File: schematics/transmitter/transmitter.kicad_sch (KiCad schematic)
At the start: 24 parts, among them Q1 2N7000, SW1 SW_Nidec_CAS-120A1, U1 PIC16F18324-xSL, U2 NRF24L01_Breakout, U3 LM2937xT

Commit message: Create gerber files and order
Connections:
- net GND: no longer RV3.S1, RV3.S2
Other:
- moved on the sheet: D1, Q1, R1, RV3

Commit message: Update
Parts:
- U3: Mfn (none) -> Texas Instruments; Mfn PN (none) -> LM2937ET-3.3/NOPB; Supplier (none) -> DigiKey; Supplier PN (none) -> LM2937ET-3.3/NOPB-ND
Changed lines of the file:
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@@
 			)
 		)
-		(property "Datasheet" "http://www.ti.com/lit/ds/symlink/lm2937.pdf"
+		(property "Datasheet" "https://www.ti.com/lit/ds/symlink/lm2937.pdf"
 			(at 133.35 130.81 0)
 			(effects
@@
 			)
 		)
-		(property "Description" "500-mA Low Dropout Regulator, TO-220"
+		(property "Description" "IC REG LINEAR 3.3V 500MA TO220-3"
 			(at 133.35 129.54 0)
 			(effects
@@
 			)
 		)
-		(property "Mfn" ""
+		(property "Mfn" "Texas Instruments"
 			(at 133.35 129.54 0)
 			(effects
@@
 			)
 		)
-		(property "Mfn PN" ""
+		(property "Mfn PN" "LM2937ET-3.3/NOPB"
 			(at 133.35 129.54 0)
 			(effects
@@
 			)
 		)
-		(property "Supplier" ""
+		(property "Supplier" "DigiKey"
 			(at 133.35 129.54 0)
 			(effects
@@
 			)
 		)
-		(property "Supplier PN" ""
+		(property "Supplier PN" "LM2937ET-3.3/NOPB-ND"
 			(at 133.35 129.54 0)
 			(effects

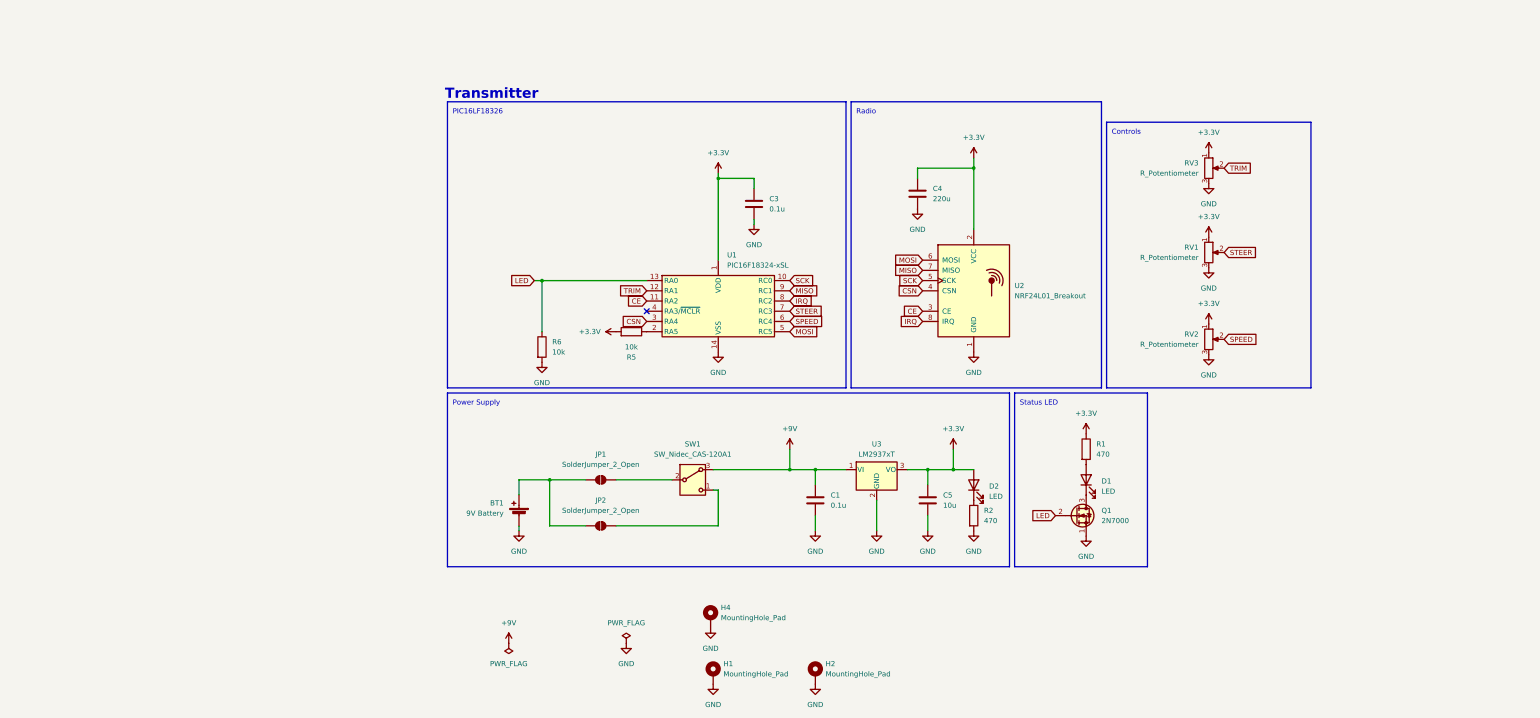
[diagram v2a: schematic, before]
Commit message: Update schematics and their images
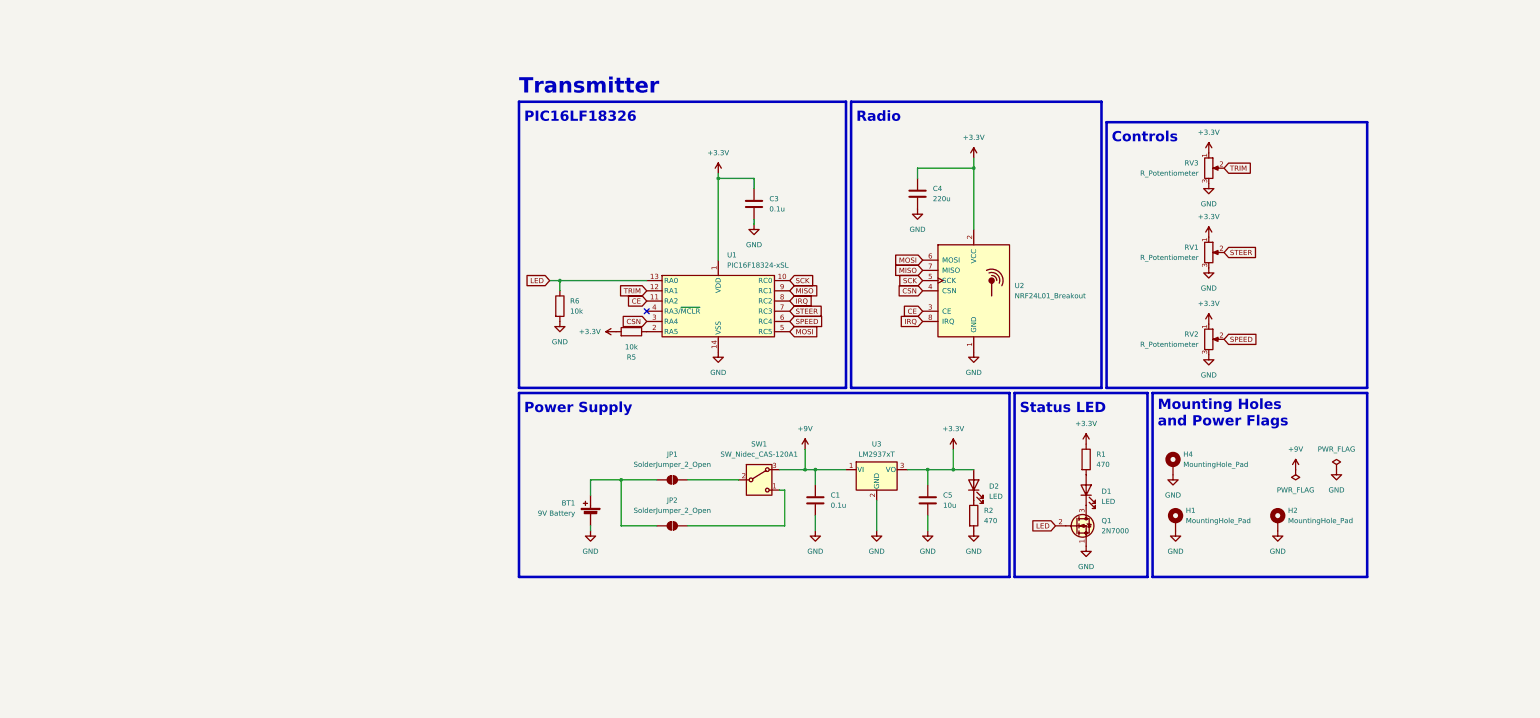
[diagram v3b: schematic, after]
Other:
- note added: "Mounting Holes and Power Flags"
- moved on the sheet: BT1, D1, H1, H2, H4, JP1, JP2, Q1, R1, R6, SW1

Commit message: Update BOM for transmitter
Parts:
- C1: Mfn (none) -> Vishay Beyschlag/Draloric/BC Components; Mfn PN (none) -> K104K15X7RF5TL2; Supplier (none) -> DigiKey; Supplier PN (none) -> BC1084TR-ND
- C4: Mfn (none) -> KEMET; Mfn PN (none) -> ESY227M035AH1AA; Supplier (none) -> DigiKey; Supplier PN (none) -> 399-6122-ND
- C5: Mfn (none) -> KEMET; Mfn PN (none) -> ESL106M100AE3AA; Supplier (none) -> DigiKey; Supplier PN (none) -> 399-15738-ND
- D1, D2: Mfn (none) -> Würth Elektronik; Mfn PN (none) -> 151051RS11000; Supplier (none) -> DigiKey; Supplier PN (none) -> 732-5016-ND
- Q1: Mfn (none) -> Diotec Semiconductor; Mfn PN (none) -> 2N7000; Supplier (none) -> DigiKey; Supplier PN (none) -> 4878-2N7000CT-ND
- R1, R2: Mfn (none) -> Stackpole Electronics Inc; Mfn PN (none) -> CF14JT470R; Supplier (none) -> DigiKey; Supplier PN (none) -> CF14JT470RTR-ND
- R5: footprint Resistor_THT:R_Axial_DIN0204_L3.6mm_D1.6mm_P7.62mm_Horizontal -> https://www.seielect.com/catalog/SEI-CF_CFM.pdf; Mfn PN (none) -> CF14JT10K0; Supplier (none) -> DigiKey; Supplier PN (none) -> CF14JT10K0TR-ND
- R6: Mfn (none) -> Stackpole Electronics Inc; Mfn PN (none) -> CF14JT10K0; Supplier (none) -> DigiKey; Supplier PN (none) -> CF14JT10K0TR-ND
- SW1: Mfn (none) -> E-Switch; Mfn PN (none) -> EG1218; Supplier (none) -> DigiKey; Supplier PN (none) -> EG1903-ND
- U2: Supplier PN (none) -> https://www.aliexpress.us/item/3256809251216534.html?src=go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

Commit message: Update images
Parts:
- BT1: Mfn (none) -> Energizer Battery Company; Mfn PN (none) -> A1604 BK210J; Supplier (none) -> DigiKey; Supplier PN (none) -> 547-A1604BK210J-ND
- C3: Mfn (none) -> Vishay Beyschlag/Draloric/BC Components; Mfn PN (none) -> K104K15X7RF5TL2; Supplier (none) -> DigiKey; Supplier PN (none) -> BC1084TR-ND
- RV1, RV2: value R_Potentiometer -> Control Pot
- RV3: value R_Potentiometer -> Trim Pot
- U1: Mfn (none) -> Microchip Technology; Mfn PN (none) -> PIC16LF18326-I/P; Supplier (none) -> DigiKey; Supplier PN (none) -> PIC16LF18326-I/P-ND
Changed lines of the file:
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@@
 			)
 		)
-		(property "Value" "R_Potentiometer"
+		(property "Value" "Trim Pot"
 			(at 213.36 55.8799 0)
 			(effects
@@
 			)
 		)
-		(property "Value" "R_Potentiometer"
+		(property "Value" "Control Pot"
 			(at 213.36 76.8349 0)
 			(effects
@@
 			)
 		)
-		(property "Datasheet" "~"
+		(property "Datasheet" "https://www.vishay.com/docs/45171/kseries.pdf"
 			(at 102.87 63.5 0)
 			(effects
@@
 			)
 		)
-		(property "Description" "Unpolarized capacitor"
+		(property "Description" "CAP CER 0.1UF 50V X7R RADIAL"
 			(at 102.87 63.5 0)
 			(effects
@@
 			)
 		)
-		(property "Mfn" ""
+		(property "Mfn" "Vishay Beyschlag/Draloric/BC Components"
 			(at 102.87 63.5 0)
 			(effects
@@
 			)
 		)
-		(property "Mfn PN" ""
+		(property "Mfn PN" "K104K15X7RF5TL2"
 			(at 102.87 63.5 0)
 			(effects
@@
 			)
 		)
-		(property "Supplier" ""
+		(property "Supplier" "DigiKey"
 			(at 102.87 63.5 0)
 			(effects
@@
 			)
 		)
-		(property "Supplier PN" ""
+		(property "Supplier PN" "BC1084TR-ND"
 			(at 102.87 63.5 0)
 			(effects
@@
 			)
 		)
-		(property "Datasheet" "~"
+		(property "Datasheet" "https://mm.digikey.com/Volume0/opasdata/d220001/medias/docus/56/A1604_DS.pdf"
 			(at 62.23 139.446 90)
 			(effects
@@
 			)
 		)
-		(property "Description" "Single-cell battery"
+		(property "Description" "BATTERY ALKALINE 9V"
 			(at 62.23 140.97 0)
 			(effects
@@
 			)
 		)
-		(property "Mfn" ""
+		(property "Mfn" "Energizer Battery Company"
 			(at 62.23 140.97 0)
 			(effects
@@
 			)
 		)
-		(property "Mfn PN" ""
+		(property "Mfn PN" "A1604 BK210J"
 			(at 62.23 140.97 0)
 			(effects
@@
 			)
 		)
-		(property "Supplier" ""
+		(property "Supplier" "DigiKey"
 			(at 62.23 140.97 0)
 			(effects
@@
 			)
 		)
-		(property "Supplier PN" ""
+		(property "Supplier PN" "547-A1604BK210J-ND"
 			(at 62.23 140.97 0)
 			(effects
@@
 			)
 		)
-		(property "Description" "PIC16F18324, 4096W FLASH, 512B SRAM, 256B EEPROM, SOIC14"
+		(property "Description" "IC MCU 8BIT 28KB FLASH 14DIP"
 			(at 93.98 90.17 0)
 			(effects
@@
 			)
 		)
-		(property "Mfn" ""
+		(property "Mfn" "Microchip Technology"
 			(at 93.98 90.17 0)
 			(effects
@@
 			)
 		)
-		(property "Mfn PN" ""
+		(property "Mfn PN" "PIC16LF18326-I/P"
 			(at 93.98 90.17 0)
 			(effects
@@
 			)
 		)
-		(property "Supplier" ""
+		(property "Supplier" "DigiKey"
 			(at 93.98 90.17 0)
 			(effects
@@
 			)
 		)
-		(property "Supplier PN" ""
+		(property "Supplier PN" "PIC16LF18326-I/P-ND"
 			(at 93.98 90.17 0)
 			(effects
@@
 			)
 		)
-		(property "Value" "R_Potentiometer"
+		(property "Value" "Control Pot"
 			(at 213.36 98.4249 0)
 			(effects
@@
 			)
 		)
-		(property "Datasheet" "RES 10K OHM 5% 1/4W AXIAL"
+		(property "Datasheet" "https://www.seielect.com/catalog/SEI-CF_CFM.pdf"
 			(at 72.39 95.25 0)
 			(effects
@@
 			(at 72.39 95.25 0)
 			(effects
-				(font
-					(size 1.27 1.27)
-				)
-				(hide yes)
-			)
-		)
-		(property "Datasheet" "https://www.seielect.com/catalog/SEI-CF_CFM.pdf"
-			(at 72.39 95.25 0)
-			(effects

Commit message: Update
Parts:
- removed C4: 220u, Capacitor_THT:CP_Radial_D5.0mm_P2.50mm, symbol Device:C
- removed JP1, JP2: SolderJumper_2_Open, Jumper:SolderJumper-2_P1.3mm_Open_RoundedPad1.0x1.5mm, symbol Jumper:SolderJumper_2_Open
- removed Q1: 2N7000, Package_TO_SOT_THT:TO-92_Inline_Wide, symbol ME218_BaseLib:2N7000
- removed R2: 470, Resistor_THT:R_Axial_DIN0204_L3.6mm_D1.6mm_P7.62mm_Horizontal, symbol Device:R
- removed U1: PIC16F18324-xSL, Package_DIP:DIP-14_W7.62mm, symbol MCU_Microchip_PIC16:PIC16F18324-xSL
- removed U3: LM2937xT, Package_TO_SOT_THT:TO-220-3_Horizontal_TabDown, symbol Regulator_Linear:LM2937xT
- added C2, C6, C8: 0.1u, Capacitor_SMD:C_0402_1005Metric, symbol ME218_BaseLib:Cap
- added C7: 10u, Capacitor_SMD:C_0402_1005Metric, symbol Device:C
- added J1: Program, Connector_PinSocket_2.54mm:PinSocket_1x05_P2.54mm_Vertical, symbol Connector:Conn_01x05_Pin
- added J2: Debug, Connector_PinSocket_2.54mm:PinSocket_1x03_P2.54mm_Vertical, symbol Connector:Conn_01x03_Pin
- added Q2: 2N7000, Package_TO_SOT_SMD:SOT-23, symbol ME218_BaseLib:2N7000
- added R3: 10k, Resistor_SMD:R_0402_1005Metric, symbol Device:R
- added R4: 1k, Resistor_SMD:R_0402_1005Metric, symbol Device:R
- added RV4: Trim Pot, Potentiometer_THT:Potentiometer_Bourns_3386P_Vertical, symbol Device:R_Potentiometer
- added SW2: ~{MCLR}, pcb_radio:SW_1825910-6-4, symbol Switch:SW_Push
- added U3: AMS1117-3.3, Package_TO_SOT_SMD:SOT-223-3_TabPin2, symbol Regulator_Linear:AMS1117-3.3
- added U4: PIC32MX170F256B, receiver:SSOP28_MC_MCH, symbol ME218_BaseLib:PIC32MX170F256B
- BT1: value 9V Battery -> Battery_Cell; Mfn Energizer Battery Company -> MPD (Memory Protection Devices); Mfn PN A1604 BK210J -> BH9VPC; Supplier PN 547-A1604BK210J-ND -> BH9V-PC-ND
- C1: value 0.1u -> 10u; footprint Capacitor_THT:CP_Radial_D5.0mm_P2.50mm -> Capacitor_SMD:C_0805_2012Metric; Mfn Vishay Beyschlag/Draloric/BC Components -> Murata Electronics; Mfn PN K104K15X7RF5TL2 -> GRM21BR71A106KA73L; Supplier PN BC1084TR-ND -> 490-10516-2-ND
- C3: value 0.1u -> 220u; footprint Capacitor_THT:CP_Radial_D5.0mm_P2.50mm -> receiver:U2-K_NCH; Mfn Vishay Beyschlag/Draloric/BC Components -> Nichicon; Mfn PN K104K15X7RF5TL2 -> UWT1C221MCL1GS; Supplier PN BC1084TR-ND -> 493-2179-2-ND
- C5: value 10u -> 22u; footprint Capacitor_THT:CP_Radial_D5.0mm_P2.50mm -> Capacitor_Tantalum_SMD:CP_EIA-2012-15_AVX-P; Mfn KEMET -> Vishay Sprague; Mfn PN ESL106M100AE3AA -> TMCP0J226MTRF; Supplier PN 399-15738-ND -> 718-2487-2-ND
- D1, D2: footprint LED_THT:LED_D5.0mm -> LED_SMD:LED_0402_1005Metric; Mfn Würth Elektronik -> QT Brightek (QTB); Mfn PN 151051RS11000 -> QBLP595-R; Supplier PN 732-5016-ND -> 1516-1217-2-ND
- R1: footprint Resistor_THT:R_Axial_DIN0204_L3.6mm_D1.6mm_P7.62mm_Horizontal -> Resistor_SMD:R_0402_1005Metric; Mfn Stackpole Electronics Inc -> YAGEO; Mfn PN CF14JT470R -> RC0402JR-07470RL; Supplier PN CF14JT470RTR-ND -> 311-470JRTR-ND
- R5: footprint https://www.seielect.com/catalog/SEI-CF_CFM.pdf -> Resistor_SMD:R_0402_1005Metric; Mfn (none) -> YAGEO; Mfn PN CF14JT10K0 -> RC0402JR-0710KL; Supplier PN CF14JT10K0TR-ND -> 311-10KJRTR-ND
- R6: value 10k -> 470; footprint Resistor_THT:R_Axial_DIN0204_L3.6mm_D1.6mm_P7.62mm_Horizontal -> Resistor_SMD:R_0402_1005Metric; Mfn Stackpole Electronics Inc -> YAGEO; Mfn PN CF14JT10K0 -> RC0402JR-07470RL; Supplier PN CF14JT10K0TR-ND -> 311-470JRTR-ND
- SW1: value SW_Nidec_CAS-120A1 -> Power
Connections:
- net +3.3V: now also R6.1, C2.2, C6.2, J1.2 (Pin_2), R3.2, RV4.1, U3.2 (VO), U4.13 (Vdd), U4.28 (AVdd); no longer D2.2 (A), R5.2
- net +9V: now also U3.3 (VI)
- net CE: now also U4.26 (RB15)
- net CSN: now also U4.23 (RB12)
- net GND: now also D1.1 (K), R5.1, C2.1, C6.1, C7.2, C8.1, J1.3 (Pin_3), J2.3 (Pin_3), Q2.2 (S), RV4.3, SW2.3, SW2.4, U3.1 (GND), U4.19 (Vss), U4.27 (AVss), U4.8 (Vss); no longer R6.2
- net IRQ: now also U4.21 (PGEC2/5VT/RB10)
- net LED: now also R5.2, Q2.1 (G), U4.6 (RB2); no longer R6.1
- net MISO: now also U4.22 (RB11)
- net MOSI: now also U4.24 (RB13)
- net SCK: now also U4.25 (RB14)
- net SPEED: now also U4.2 (RA0)
- net STEER: now also U4.10 (RA3)
- net at D2.1 (K): now also Q2.3 (D)
- net at SW1.2 (B): now also BT1.1 (+)
- net TRIM renamed STEER_TRIM
- net STEER_TRIM: now also U4.9 (RA2)
- new net: C8.2, R3.1, R4.2, SW2.1, SW2.2
- new net: C7.1, U4.20 (Vcap)
- new net: D2.2 (A), R6.2
- new net PGClk: J1.5 (Pin_5), U4.5 (PGEC1/RB1)
- new net PGData: J1.4 (Pin_4), U4.4 (PGED1/RB0)
- new net RXD: J2.2 (Pin_2), U4.16 (5VT/RB7)
- new net SPEED_TRIM: RV4.2, U4.3 (RA1)
- new net TXD: J2.1 (Pin_1), U4.15 (PGEC3/5VT/RB6)
- new net ~{MCLR}: J1.1 (Pin_1), R4.1, U4.1 (~{MCLR})
- no-connect marks 1 -> 7
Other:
- note added: "MCU"
- note added: "Program and Debug"
- note added: "Reset Buttons"
- note removed: "PIC16LF18326"

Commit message: Update
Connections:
- net +9V: now also SW1.2 (B); no longer SW1.3 (A)
- net GND: now also SW1.1 (C)
- net at BT1.1 (+): now also SW1.3 (A); no longer SW1.2 (B)
- no-connect marks 7 -> 6
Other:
- note added: "Control Trims"
- moved on the sheet: BT1, C1, C2, C5, C6, C7, C8, D1, D2, J1, J2, Q2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

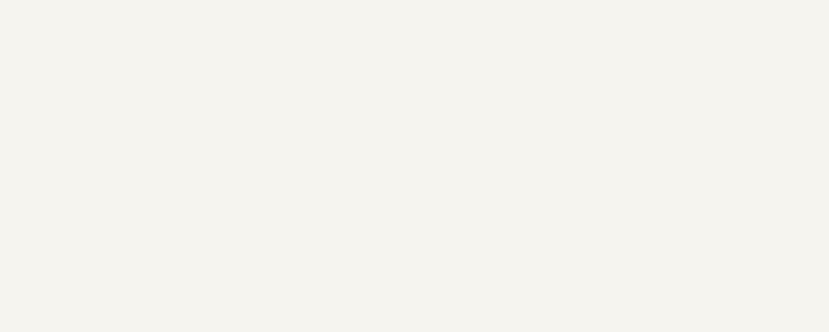
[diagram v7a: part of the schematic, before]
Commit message: Mark changes on kicad
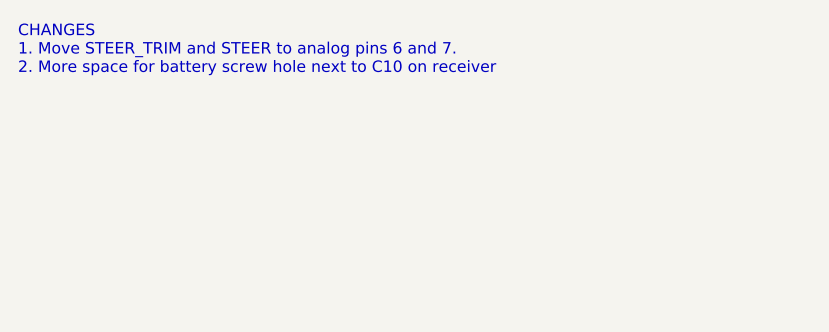
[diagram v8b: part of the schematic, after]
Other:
- note added: "CHANGES 1. Move STEER_TRIM and STEER to analog pins 6 and 7. 2. More space for battery screw hole next to C10 on receiver"
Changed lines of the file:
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@@
+		)
+	)
+	(text "CHANGES\n1. Move STEER_TRIM and STEER to analog pins 6 and 7.\n2. More space for battery screw hole next to C10 on receiver"
+		(exclude_from_sim no)
+		(at -82.55 18.415 0)
+		(effects
+			(font
+				(size 1.27 1.27)
+			)
+			(justify left)
 		)
 	)
